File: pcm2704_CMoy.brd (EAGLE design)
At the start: 100.3 x 77.5 mm, 85 parts, among them IC3 7815DT, IC4 tsr 1-2433, IC5 7915TV, Q1 12MHz, U1 PCM2704, U2 OPA2134P, U3 TC962EPA, X2 PN61729-S, X5 22-23-2031, X6 22-23-2031

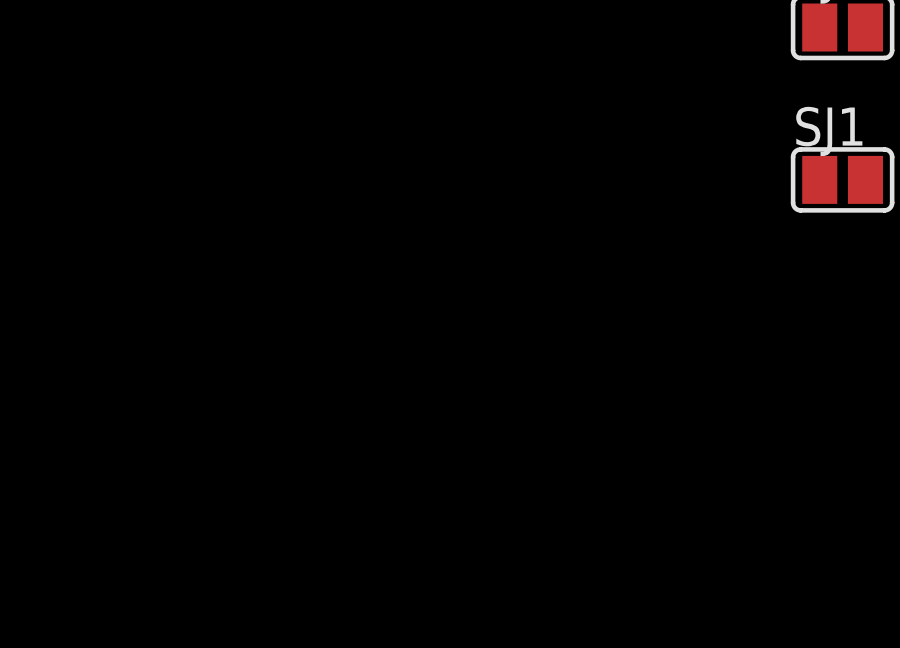
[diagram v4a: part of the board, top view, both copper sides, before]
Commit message: - Added D+ pullup activator transistor
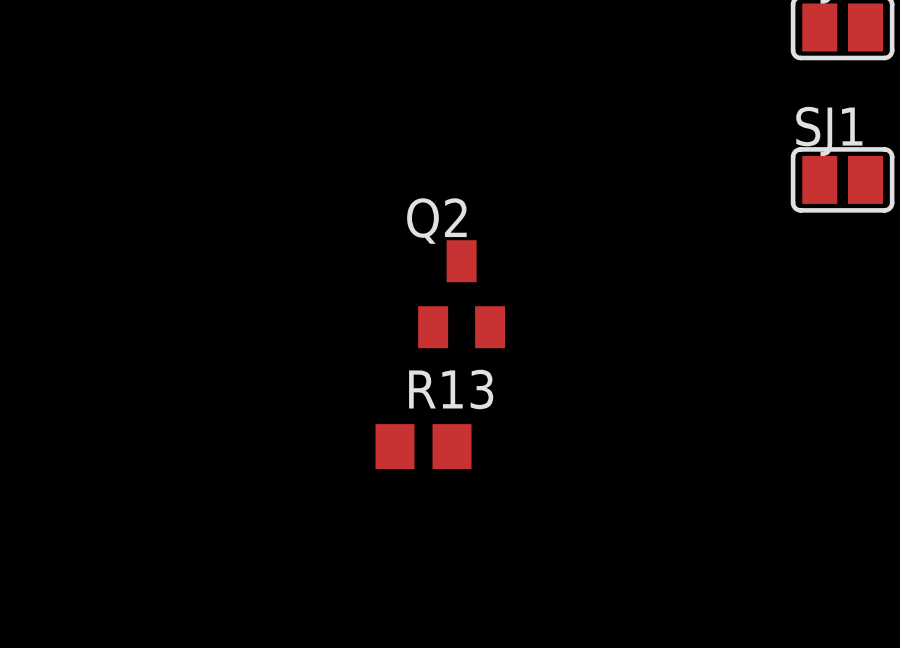
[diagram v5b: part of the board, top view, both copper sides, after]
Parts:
- added Q2: (no value), semicon-smd-ipc:SOT23
- added R13: 10K, rcl:R0805
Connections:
- new net N$38: Q2.1, R13.2
- new net N$39: Q2.2, R2.2
- net +3V3: now also Q2.3
- net VBUS: now also R13.1
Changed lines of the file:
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@@
 <element name="CN2" library="microbuilder" package="4UCONN_05550" value="" x="96.52" y="11.43" rot="R180"/>
 <element name="R12" library="rcl" package="M0805" value="1M" x="19.05" y="19.05" rot="R180"/>
+<element name="Q2" library="semicon-smd-ipc" package="SOT23" value="" x="-24.13" y="-26.67"/>
+<element name="R13" library="rcl" package="R0805" value="10K" x="-25.4" y="-31.75"/>
 </elements>
 <signals>
@@
 <contactref element="R12" pad="1"/>
 <contactref element="VBUS" pad="TP"/>
-<wire x1="21.59" y1="16.51" x2="20" y2="19.05" width="0" layer="19" extent="1-1"/>
-<wire x1="31.904" y1="-16.185" x2="21.59" y2="16.51" width="0" layer="19" extent="1-1"/>
+<contactref element="R13" pad="1"/>
+<wire x1="31.904" y1="-16.185" x2="-26.35" y2="-31.75" width="0" layer="19" extent="1-1"/>
+<wire x1="21.59" y1="16.51" x2="31.904" y2="-16.185" width="0" layer="19" extent="1-1"/>
+<wire x1="20" y1="19.05" x2="21.59" y2="16.51" width="0" layer="19" extent="1-1"/>
 </signal>
 <signal name="GND">
@@
 <contactref element="X6" pad="3"/>
 <contactref element="P1" pad="G2"/>
-<wire x1="83.82" y1="71.12" x2="90.17" y2="59.69" width="0" layer="19" extent="1-1"/>
+<wire x1="90.17" y1="59.69" x2="83.82" y2="71.12" width="0" layer="19" extent="1-1"/>
 <wire x1="40.132" y1="56.515" x2="83.82" y2="71.12" width="0" layer="19" extent="1-1"/>
 <wire x1="38.1" y1="63.5" x2="40.132" y2="56.515" width="0" layer="19" extent="1-1"/>
@@
 <contactref element="X6" pad="1"/>
 <contactref element="P1" pad="G1"/>
-<wire x1="88.9" y1="71.12" x2="92.71" y2="59.69" width="0" layer="19" extent="1-1"/>
+<wire x1="92.71" y1="59.69" x2="88.9" y2="71.12" width="0" layer="19" extent="1-1"/>
 <wire x1="35.56" y1="69.85" x2="88.9" y2="71.12" width="0" layer="19" extent="1-1"/>
 <wire x1="27.94" y1="63.5" x2="35.56" y2="69.85" width="0" layer="19" extent="1-1"/>
@@
 <contactref element="R43L" pad="1"/>
 <contactref element="CN2" pad="3"/>
-<wire x1="91.44" y1="24.13" x2="87.22" y2="10.33" width="0" layer="19" extent="1-1"/>
 <wire x1="87.63" y1="24.13" x2="91.44" y2="24.13" width="0" layer="19" extent="1-1"/>
+<wire x1="87.22" y1="10.33" x2="87.63" y2="24.13" width="0" layer="19" extent="1-1"/>
 </signal>
 <signal name="AMP_OUT_LEFT">
@@
 <contactref element="C41L" pad="2"/>
 <contactref element="R41L" pad="1"/>
-<wire x1="85.09" y1="31.75" x2="57.15" y2="38.354" width="0" layer="19" extent="1-1"/>
-<wire x1="82.55" y1="34.29" x2="85.09" y2="31.75" width="0" layer="19" extent="1-1"/>
+<wire x1="85.09" y1="31.75" x2="82.55" y2="34.29" width="0" layer="19" extent="1-1"/>
+<wire x1="57.15" y1="38.354" x2="82.55" y2="34.29" width="0" layer="19" extent="1-1"/>
 </signal>
 <signal name="N$18">
@@
 <contactref element="U2" pad="3"/>
 <contactref element="R41R" pad="2"/>
-<wire x1="83.82" y1="54.61" x2="71.12" y2="38.354" width="0" layer="19" extent="1-1"/>
 <wire x1="85.09" y1="41.91" x2="83.82" y2="54.61" width="0" layer="19" extent="1-1"/>
+<wire x1="71.12" y1="38.354" x2="85.09" y2="41.91" width="0" layer="19" extent="1-1"/>
 </signal>
 <signal name="N$19">
 <contactref element="C41R" pad="1"/>
 <contactref element="P1" pad="O2"/>
-<wire x1="90.17" y1="62.23" x2="71.12" y2="65.786" width="0" layer="19" extent="1-1"/>
+<wire x1="71.12" y1="65.786" x2="90.17" y2="62.23" width="0" layer="19" extent="1-1"/>
 </signal>
 <signal name="N$21">
@@
 <contactref element="R21" pad="2"/>
 <contactref element="LED1" pad="A"/>
-<wire x1="67.31" y1="73.66" x2="63.5" y2="72.39" width="0" layer="19" extent="1-1"/>
+<wire x1="63.5" y1="72.39" x2="67.31" y2="73.66" width="0" layer="19" extent="1-1"/>
 </signal>
 <signal name="N$9">
@@
 <contactref element="C4" pad="2"/>
 <contactref element="EXTROM" pad="1"/>
-<wire x1="-5.08" y1="31.75" x2="-5.08" y2="39.37" width="0" layer="19" extent="1-1"/>
-<wire x1="28.575" y1="-10.48" x2="-5.08" y2="31.75" width="0" layer="19" extent="1-1"/>
-<wire x1="31.904" y1="-12.935" x2="28.575" y2="-10.48" width="0" layer="19" extent="1-1"/>
-<wire x1="31.904" y1="-15.535" x2="31.904" y2="-12.935" width="0" layer="19" extent="1-1"/>
-<wire x1="31.904" y1="-18.785" x2="31.904" y2="-15.535" width="0" layer="19" extent="1-1"/>
+<contactref element="Q2" pad="3"/>
+<wire x1="13.97" y1="-30.48" x2="-24.13" y2="-25.57" width="0" layer="19" extent="1-1"/>
+<wire x1="28.575" y1="-17.46" x2="13.97" y2="-30.48" width="0" layer="19" extent="1-1"/>
+<wire x1="31.904" y1="-18.785" x2="28.575" y2="-17.46" width="0" layer="19" extent="1-1"/>
 <wire x1="31.904" y1="-19.435" x2="31.904" y2="-18.785" width="0" layer="19" extent="1-1"/>
-<wire x1="28.575" y1="-17.46" x2="31.904" y2="-18.785" width="0" layer="19" extent="1-1"/>
+<wire x1="31.904" y1="-15.535" x2="31.904" y2="-18.785" width="0" layer="19" extent="1-1"/>
+<wire x1="31.904" y1="-12.935" x2="31.904" y2="-15.535" width="0" layer="19" extent="1-1"/>
+<wire x1="28.575" y1="-10.48" x2="31.904" y2="-12.935" width="0" layer="19" extent="1-1"/>
 <wire x1="39.216" y1="-12.935" x2="31.904" y2="-12.935" width="0" layer="19" extent="1-1"/>
 <wire x1="39.216" y1="-14.885" x2="39.216" y2="-12.935" width="0" layer="19" extent="1-1"/>
@@
 <wire x1="43.18" y1="-20.64" x2="39.216" y2="-16.835" width="0" layer="19" extent="1-1"/>
 <wire x1="46.355" y1="-20.64" x2="43.18" y2="-20.64" width="0" layer="19" extent="1-1"/>
-<wire x1="13.97" y1="-30.48" x2="28.575" y2="-17.46" width="0" layer="19" extent="1-1"/>
+<wire x1="-5.08" y1="31.75" x2="28.575" y2="-10.48" width="0" layer="19" extent="1-1"/>
+<wire x1="-5.08" y1="39.37" x2="-5.08" y2="31.75" width="0" layer="19" extent="1-1"/>
 </signal>
 <signal name="SUSPEND">
@@
 <contactref element="U2" pad="1"/>
 <contactref element="RSUPP_R" pad="2"/>
-<wire x1="93.98" y1="39.37" x2="90.17" y2="41.91" width="0" layer="19" extent="1-1"/>
+<wire x1="90.17" y1="41.91" x2="93.98" y2="39.37" width="0" layer="19" extent="1-1"/>
 </signal>
 <signal name="N$35">
 <contactref element="U2" pad="7"/>
 <contactref element="RSUPP_L" pad="2"/>
-<wire x1="91.44" y1="31.75" x2="87.63" y2="34.29" width="0" layer="19" extent="1-1"/>
+<wire x1="87.63" y1="34.29" x2="91.44" y2="31.75" width="0" layer="19" extent="1-1"/>
 </signal>
 <signal name="N$13">
@@
 <wire x1="14.87" y1="13.99" x2="18.1" y2="19.05" width="0" layer="19" extent="1-1"/>
 </signal>
+<signal name="N$38">
+<contactref element="R13" pad="2"/>
+<contactref element="Q2" pad="1"/>
+<wire x1="-25.08" y1="-27.77" x2="-24.45" y2="-31.75" width="0" layer="19" extent="1-1"/>
+</signal>
+<signal name="N$39">
+<contactref element="Q2" pad="2"/>
+<contactref element="R2" pad="2"/>
+<wire x1="26.99" y1="-20.32" x2="-23.18" y2="-27.77" width="0" layer="19" extent="1-1"/>
+</signal>
 </signals>
